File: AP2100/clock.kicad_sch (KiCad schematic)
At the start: 53 parts

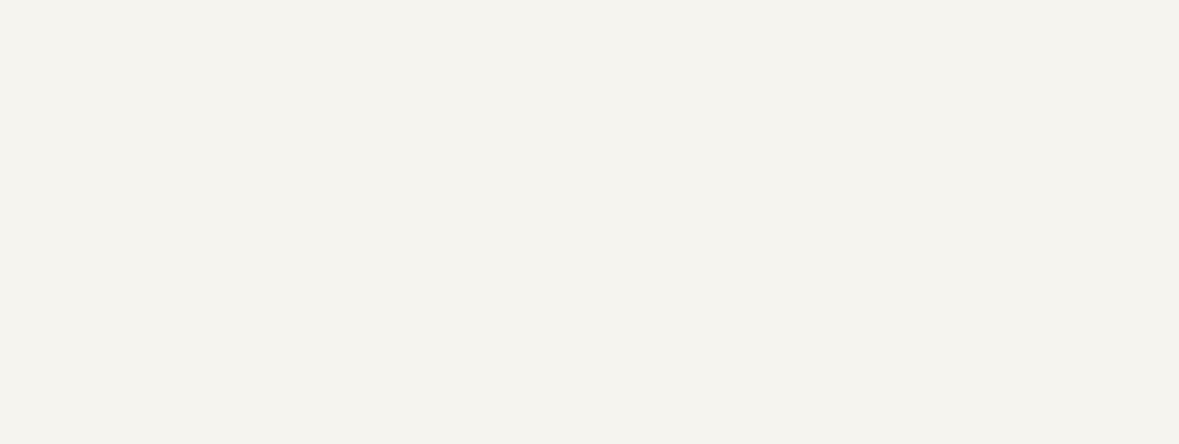
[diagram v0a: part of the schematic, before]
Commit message: Mostly done with USB - USB1 complete just duplicate to 2+3
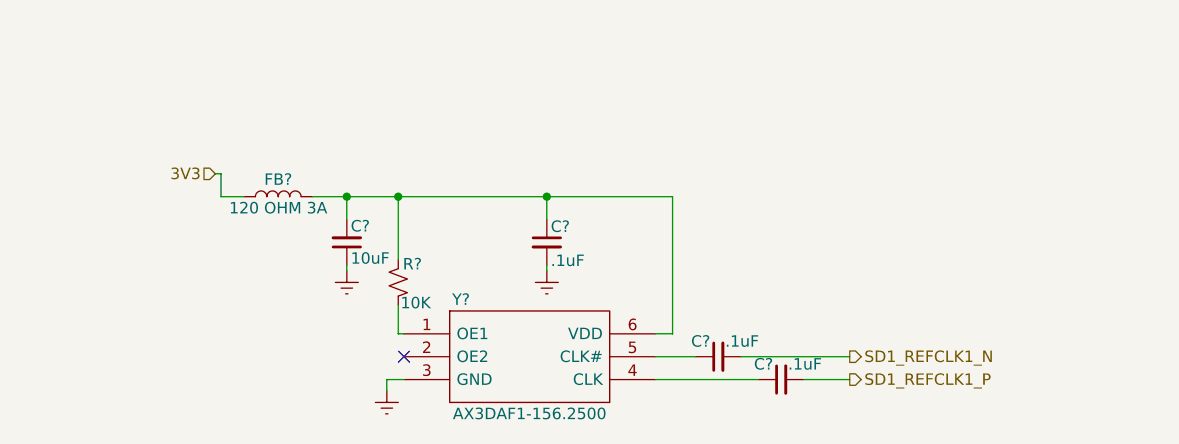
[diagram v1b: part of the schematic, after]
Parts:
- added C?: 10uF, Capacitor_SMD:C_0805_2012Metric, symbol Device:C_Small
- added C? (x3): .1uF, Capacitor_SMD:C_0402_1005Metric, symbol Device:C_Small
- added FB?: 120 OHM 3A, Inductor_SMD:L_0603_1608Metric, symbol Device:L
- added R?: 10K, Resistor_SMD:R_0402_1005Metric, symbol Device:R_Small_US
- added Y?: AX3DAF1-156.2500, AX3DCF11562500, symbol AX3DCF1-156.2500:AX3DCF1-156.2500
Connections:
- net 3V3: now also FB?.1
- net GND: now also C?.1, C?.2, Y?.3 (GND)
- new net: R?.1, Y?.1 (OE1)
- new net: C?.1, C?.2, FB?.2, R?.2, Y?.6 (VDD)
- new net: C?.1, Y?.5 (CLK#)
- new net: C?.1, Y?.4 (CLK)
- new net SD1_REFCLK1_N: C?.2
- new net SD1_REFCLK1_P: C?.2
- no-connect marks 8 -> 9

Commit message: Annotate and update PCB with current design
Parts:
- gave numbers to parts that had none: 60

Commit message: Review / cleanup footprints, etc
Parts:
- renumbered C163 to C128, C164 to C129, C165 to C130, C166 to C131, C167 to C132, C168 to C133, C169 to C134, C170 to C135, C171 to C136, C172 to C137, C173 to C138, C174 to C139, C175 to C140, C176 to C141, C177 to C142, C178 to C143, C179 to C144, C180 to C145, C181 to C146, C182 to C147, C183 to C148, R69 to R55, R70 to R56, R71 to R57, R72 to R58, R73 to R59, R74 to R60, R75 to R61, R76 to R62, R77 to R63, R78 to R64, R79 to R65, R80 to R66, R81 to R67, R82 to R68, R83 to R69, R84 to R70, R85 to R71, R86 to R72, R87 to R73, R88 to R74, R89 to R75, R90 to R76, R91 to R77, R92 to R78, R93 to R79, R94 to R80, R95 to R81, R96 to R82, R97 to R83, R98 to R84, R99 to R85, R100 to R86, R101 to R87, R102 to R88
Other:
- note added: "SERDES 10G Clock"

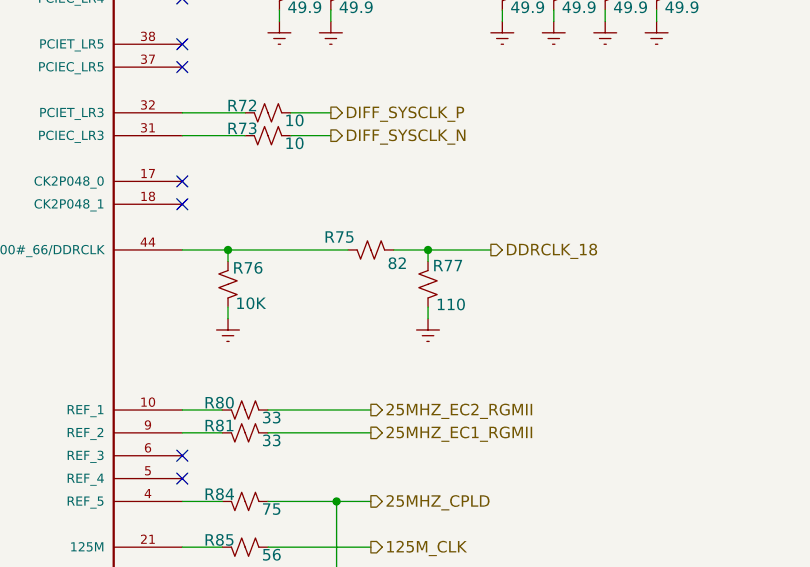
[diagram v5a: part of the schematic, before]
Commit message: Added Thermal solutions PDF Fix DDRCLK pulldown
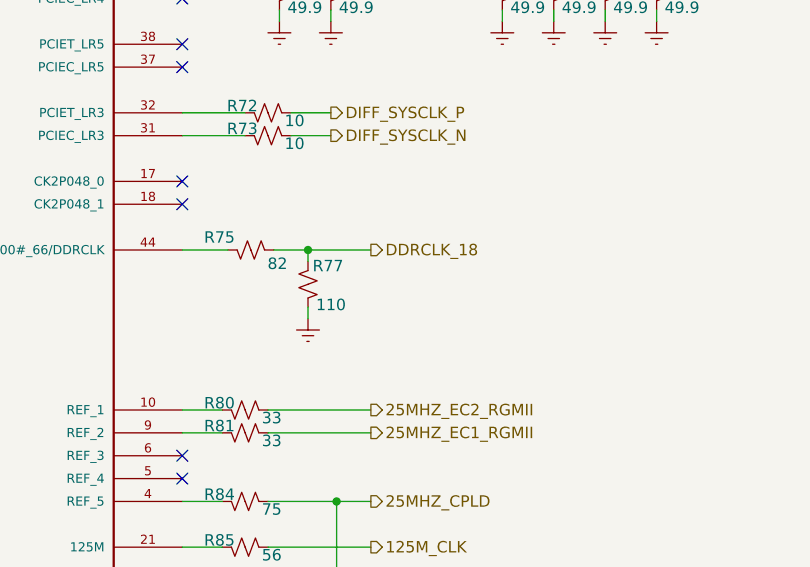
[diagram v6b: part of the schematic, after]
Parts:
- removed R76: 10K, Resistor_SMD:R_0402_1005Metric, symbol Device:R_Small_US
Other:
- moved on the sheet: R75, R77

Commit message: More cleanups
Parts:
- renumbered R77 to R76, R78 to R77, R79 to R78, R80 to R79, R81 to R80, R82 to R81, R83 to R82, R84 to R83, R85 to R84, R86 to R85, R87 to R86, R88 to R87
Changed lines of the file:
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@@
   (symbol (lib_id "AP2100-rescue:GND-Scott") (at 43.18 41.275 0) (unit 1)
     (in_bom yes) (on_board yes)
-    (property "Reference" "#PWR071" (id 0) (at 43.18 47.625 0)
+    (property "Reference" "#PWR072" (id 0) (at 43.18 47.625 0)
       (effects (font (size 1.27 1.27)) hide)
     )
@@
   (symbol (lib_id "AP2100-rescue:GND-Scott") (at 56.515 100.33 0) (unit 1)
     (in_bom yes) (on_board yes)
-    (property "Reference" "#PWR083" (id 0) (at 56.515 106.68 0)
+    (property "Reference" "#PWR084" (id 0) (at 56.515 106.68 0)
       (effects (font (size 1.27 1.27)) hide)
     )
@@
   (symbol (lib_id "AP2100-rescue:GND-Scott") (at 64.135 39.37 0) (unit 1)
     (in_bom yes) (on_board yes)
-    (property "Reference" "#PWR070" (id 0) (at 64.135 45.72 0)
+    (property "Reference" "#PWR071" (id 0) (at 64.135 45.72 0)
       (effects (font (size 1.27 1.27)) hide)
     )
@@
   (symbol (lib_id "AP2100-rescue:GND-Scott") (at 84.455 37.465 0) (unit 1)
     (in_bom yes) (on_board yes)
-    (property "Reference" "#PWR069" (id 0) (at 84.455 43.815 0)
+    (property "Reference" "#PWR070" (id 0) (at 84.455 43.815 0)
       (effects (font (size 1.27 1.27)) hide)
     )
@@
   (symbol (lib_id "AP2100-rescue:GND-Scott") (at 94.615 63.5 0) (unit 1)
     (in_bom yes) (on_board yes)
-    (property "Reference" "#PWR073" (id 0) (at 94.615 69.85 0)
+    (property "Reference" "#PWR074" (id 0) (at 94.615 69.85 0)
       (effects (font (size 1.27 1.27)) hide)
     )
@@
   (symbol (lib_id "AP2100-rescue:GND-Scott") (at 94.615 73.66 0) (unit 1)
     (in_bom yes) (on_board yes)
-    (property "Reference" "#PWR080" (id 0) (at 94.615 80.01 0)
+    (property "Reference" "#PWR081" (id 0) (at 94.615 80.01 0)
       (effects (font (size 1.27 1.27)) hide)
     )
@@
   (symbol (lib_id "AP2100-rescue:GND-Scott") (at 94.615 83.82 0) (unit 1)
     (in_bom yes) (on_board yes)
-    (property "Reference" "#PWR081" (id 0) (at 94.615 90.17 0)
+    (property "Reference" "#PWR082" (id 0) (at 94.615 90.17 0)
       (effects (font (size 1.27 1.27)) hide)
     )
@@
   (symbol (lib_id "AP2100-rescue:GND-Scott") (at 94.615 93.98 0) (unit 1)
     (in_bom yes) (on_board yes)
-    (property "Reference" "#PWR082" (id 0) (at 94.615 100.33 0)
+    (property "Reference" "#PWR083" (id 0) (at 94.615 100.33 0)
       (effects (font (size 1.27 1.27)) hide)
     )
@@
   (symbol (lib_id "AP2100-rescue:GND-Scott") (at 178.435 67.31 0) (unit 1)
     (in_bom yes) (on_board yes)
-    (property "Reference" "#PWR074" (id 0) (at 178.435 73.66 0)
+    (property "Reference" "#PWR075" (id 0) (at 178.435 73.66 0)
       (effects (font (size 1.27 1.27)) hide)
     )
@@
   (symbol (lib_id "AP2100-rescue:GND-Scott") (at 184.15 67.31 0) (unit 1)
     (in_bom yes) (on_board yes)
-    (property "Reference" "#PWR075" (id 0) (at 184.15 73.66 0)
+    (property "Reference" "#PWR076" (id 0) (at 184.15 73.66 0)
       (effects (font (size 1.27 1.27)) hide)
     )
@@
   (symbol (lib_id "AP2100-rescue:GND-Scott") (at 203.2 67.31 0) (unit 1)
     (in_bom yes) (on_board yes)
-    (property "Reference" "#PWR076" (id 0) (at 203.2 73.66 0)
+    (property "Reference" "#PWR077" (id 0) (at 203.2 73.66 0)
       (effects (font (size 1.27 1.27)) hide)
     )
@@
   (symbol (lib_id "AP2100-rescue:GND-Scott") (at 208.915 67.31 0) (unit 1)
     (in_bom yes) (on_board yes)
-    (property "Reference" "#PWR077" (id 0) (at 208.915 73.66 0)
+    (property "Reference" "#PWR078" (id 0) (at 208.915 73.66 0)
       (effects (font (size 1.27 1.27)) hide)
     )
@@
   (symbol (lib_id "AP2100-rescue:GND-Scott") (at 214.63 67.31 0) (unit 1)
     (in_bom yes) (on_board yes)
-    (property "Reference" "#PWR078" (id 0) (at 214.63 73.66 0)
+    (property "Reference" "#PWR079" (id 0) (at 214.63 73.66 0)
       (effects (font (size 1.27 1.27)) hide)
     )
@@
   (symbol (lib_id "AP2100-rescue:GND-Scott") (at 220.345 67.31 0) (unit 1)
     (in_bom yes) (on_board yes)
-    (property "Reference" "#PWR079" (id 0) (at 220.345 73.66 0)
+    (property "Reference" "#PWR080" (id 0) (at 220.345 73.66 0)
       (effects (font (size 1.27 1.27)) hide)
     )
@@
   (symbol (lib_id "AP2100-rescue:GND-Scott") (at 244.475 41.91 0) (unit 1)
     (in_bom yes) (on_board yes)
-    (property "Reference" "#PWR072" (id 0) (at 244.475 48.26 0)
+    (property "Reference" "#PWR073" (id 0) (at 244.475 48.26 0)
       (effects (font (size 1.27 1.27)) hide)
     )
@@
   (symbol (lib_id "Device:R_Small_US") (at 83.185 114.3 0) (mirror y) (unit 1)
     (in_bom yes) (on_board yes)
-    (property "Reference" "R82" (id 0) (at 87.122 112.522 0)
+    (property "Reference" "R81" (id 0) (at 87.122 112.522 0)
       (effects (font (size 1.27 1.27)) (justify left))
     )
@@
   (symbol (lib_id "Device:R_Small_US") (at 83.185 193.04 0) (mirror x) (unit 1)
     (in_bom yes) (on_board yes)
-    (property "Reference" "R88" (id 0) (at 83.693 191.008 0)
+    (property "Reference" "R87" (id 0) (at 83.693 191.008 0)
       (effects (font (size 1.27 1.27)) (justify left))
     )
@@
   (symbol (lib_id "Device:R_Small_US") (at 86.995 132.08 0) (mirror y) (unit 1)
     (in_bom yes) (on_board yes)
-    (property "Reference" "R87" (id 0) (at 90.932 130.302 0)
+    (property "Reference" "R86" (id 0) (at 90.932 130.302 0)
       (effects (font (size 1.27 1.27)) (justify left))
     )
@@
   (symbol (lib_id "Device:R_Small_US") (at 89.535 114.3 0) (mirror y) (unit 1)
     (in_bom yes) (on_board yes)
-    (property "Reference" "R83" (id 0) (at 93.472 112.522 0)
+    (property "Reference" "R82" (id 0) (at 93.472 112.522 0)
       (effects (font (size 1.27 1.27)) (justify left))
     )
@@
   (symbol (lib_id "Device:R_Small_US") (at 98.425 105.41 90) (mirror x) (unit 1)
     (in_bom yes) (on_board yes)
-    (property "Reference" "R78" (id 0) (at 96.647 106.553 90)
+    (property "Reference" "R77" (id 0) (at 96.647 106.553 90)
       (effects (font (size 1.27 1.27)) (justify left))
     )
@@
   (symbol (lib_id "Device:R_Small_US") (at 98.425 107.95 90) (mirror x) (unit 1)
     (in_bom yes) (on_board yes)
-    (property "Reference" "R79" (id 0) (at 96.647 109.093 90)
+    (property "Reference" "R78" (id 0) (at 96.647 109.093 90)
       (effects (font (size 1.27 1.27)) (justify left))
     )
@@
   (symbol (lib_id "Device:R_Small_US") (at 174.625 110.49 90) (mirror x) (unit 1)
     (in_bom yes) (on_board yes)
-    (property "Reference" "R80" (id 0) (at 173.482 109.728 90)
+    (property "Reference" "R79" (id 0) (at 173.482 109.728 90)
       (effects (font (size 1.27 1.27)) (justify left))
     )
@@
   (symbol (lib_id "Device:R_Small_US") (at 174.625 113.03 90) (mirror x) (unit 1)
     (in_bom yes) (on_board yes)
-    (property "Reference" "R81" (id 0) (at 173.482 112.268 90)
+    (property "Reference" "R80" (id 0) (at 173.482 112.268 90)
       (effects (font (size 1.27 1.27)) (justify left))
     )
@@
   (symbol (lib_id "Device:R_Small_US") (at 174.625 120.65 90) (mirror x) (unit 1)
     (in_bom yes) (on_board yes)
-    (property "Reference" "R84" (id 0) (at 173.482 119.888 90)
+    (property "Reference" "R83" (id 0) (at 173.482 119.888 90)
       (effects (font (size 1.27 1.27)) (justify left))
     )
@@
   (symbol (lib_id "Device:R_Small_US") (at 174.625 125.73 90) (mirror x) (unit 1)
     (in_bom yes) (on_board yes)
-    (property "Reference" "R85" (id 0) (at 173.482 124.968 90)
+    (property "Reference" "R84" (id 0) (at 173.482 124.968 90)
       (effects (font (size 1.27 1.27)) (justify left))
     )
@@
   (symbol (lib_id "Device:R_Small_US") (at 181.61 96.52 0) (mirror x) (unit 1)
     (in_bom yes) (on_board yes)
-    (property "Reference" "R77" (id 0) (at 182.118 94.488 0)
+    (property "Reference" "R76" (id 0) (at 182.118 94.488 0)
       (effects (font (size 1.27 1.27)) (justify left))
     )
@@
   (symbol (lib_id "Device:R_Small_US") (at 184.785 131.445 0) (mirror x) (unit 1)
     (in_bom yes) (on_board yes)
-    (property "Reference" "R86" (id 0) (at 185.293 129.413 0)
-      (effects (font (size 1.27 1.27)) (justify left))
-    )
+    (property "Reference" "R85" (id 0) (at 185.293 129.413 0)
+      (effects (font (size 1.27 1.27)) (justify left))
+    )

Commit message: Not sure
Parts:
- U8: PartsBoxID (none) -> 6V49205BNLGI
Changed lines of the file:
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@@
   (junction (at 220.345 49.53) (diameter 0.9144) (color 0 0 0 0))
   (junction (at 244.475 34.29) (diameter 0.9144) (color 0 0 0 0))
+  (no_connect (at 167.64 87.63))
+  (no_connect (at 167.64 69.85))
+  (no_connect (at 167.64 115.57))
+  (no_connect (at 167.64 72.39))
   (no_connect (at 167.64 64.77))
-  (no_connect (at 167.64 69.85))
   (no_connect (at 167.64 62.23))
-  (no_connect (at 167.64 72.39))
-  (no_connect (at 167.64 87.63))
   (no_connect (at 167.64 85.09))
+  (no_connect (at 83.82 201.295))
   (no_connect (at 167.64 118.11))
-  (no_connect (at 83.82 201.295))
-  (no_connect (at 167.64 115.57))
   (wire (pts (xy 41.275 93.98) (xy 41.275 99.06))
     (stroke (width 0) (type solid) (color 0 0 0 0))
@@
       (effects (font (size 1.27 1.27)) (justify left bottom) hide)
     )
-  )
+    (property "PartsBoxID" "6V49205BNLGI" (id 4) (at 134.62 90.17 0)
+      (effects (font (size 1.27 1.27)) hide)
+    )
+  )
